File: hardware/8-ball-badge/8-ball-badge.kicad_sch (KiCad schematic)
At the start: 76 parts, among them J1 BattConn, J2 SAO Header 1, J3 SAO Header 2, Q1 AO3401A, Q2 S8050, SW1 SW_Push, SW2 TS-1187A-B-A-B, U1 TC4056A, U10 ME6210A33PG, U2 W25Q128JVSIQTR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

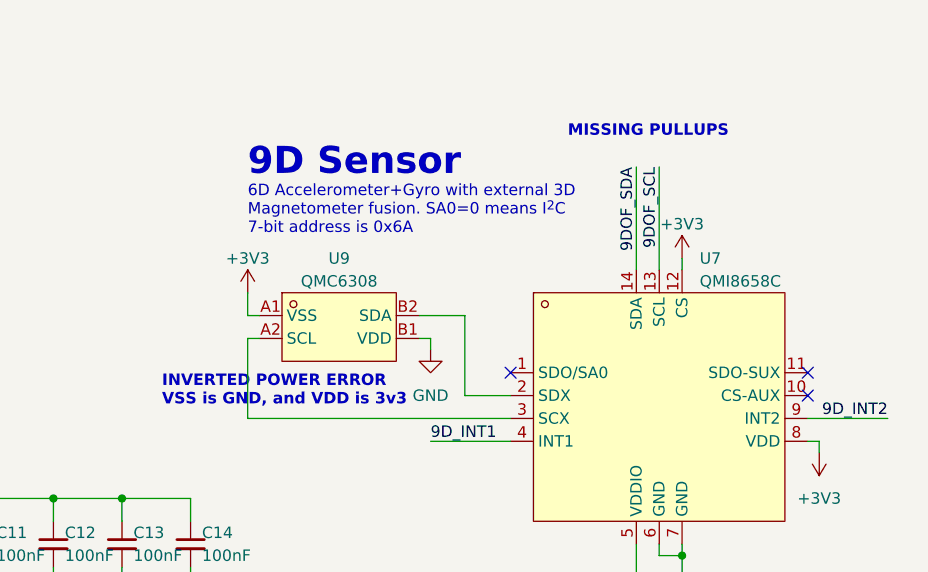
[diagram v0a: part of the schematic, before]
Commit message: Fix issues with 9DoF chip
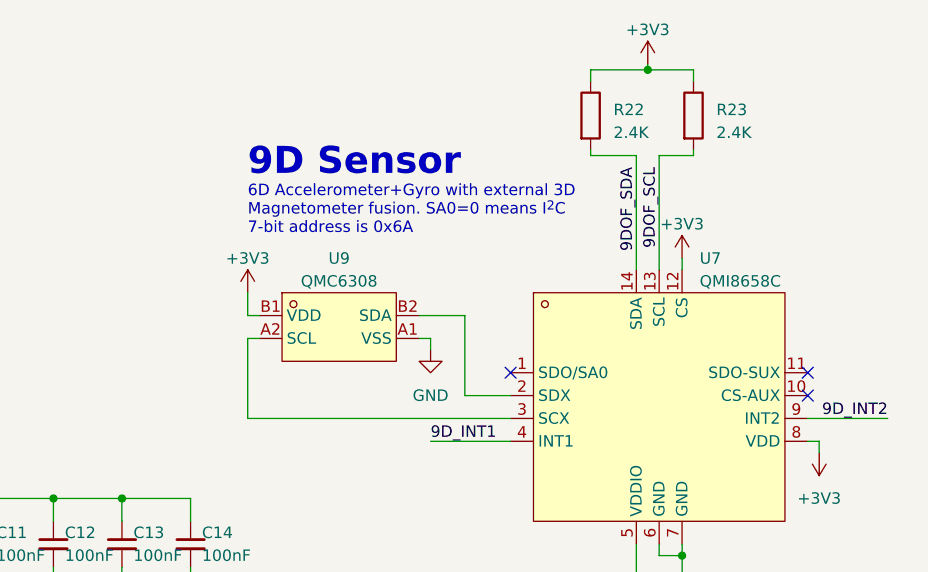
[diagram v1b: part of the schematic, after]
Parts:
- added R22, R23: 2.4K, Resistor_SMD:R_0603_1608Metric_Pad0.98x0.95mm_HandSolder, symbol Device:R
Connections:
- net +3V3: now also U9.B1 (VDD), R22.1, R23.1; no longer U9.A1 (VSS)
- net 9DOF_SCL: now also R23.2
- net 9DOF_SDA: now also R22.2
- net GND: now also U9.A1 (VSS); no longer U9.B1 (VDD)
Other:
- note removed: "INVERTED POWER ERROR VSS is GND, and VDD is 3v3"
- note removed: "MISSING PULLUPS"
- company: (none) -> Designed by Tyler Crumpton (CrumpSpace)
- title: (none) -> Magic 8-Badge
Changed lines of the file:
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@@
 (kicad_sch (version 20230121) (generator eeschema)
   (paper "A3")
+  (title_block
+    (title "Magic 8-Badge")
+    (date "2023-11-04")
+    (rev "v1 ")
+    (company "Designed by Tyler Crumpton (CrumpSpace)")
+    (comment 1 "Copyright Tyler Crumpton, 2023 ")
+    (comment 2 "Licensed under CERN-OHL-P version 2")
+    (comment 3 "PhreakNIC 2023 Edition")
+  )
   (junction (at 289.56 176.53) (diameter 0) (color 0 0 0 0)
   )
@@
   (junction (at 215.9 115.57) (diameter 0) (color 0 0 0 0)
   )
+  (junction (at 234.95 20.955) (diameter 0) (color 0 0 0 0)
+  )
   (junction (at 43.18 160.02) (diameter 0) (color 0 0 0 0)
   )
@@
     (stroke (width 0) (type default))
   )
+  (wire (pts (xy 234.95 20.955) (xy 234.95 20.32))
+    (stroke (width 0) (type default))
+  )
   (wire (pts (xy 271.78 72.39) (xy 271.78 73.66))
     (stroke (width 0) (type default))
@@
     (stroke (width 0) (type default))
   )
+  (wire (pts (xy 240.03 30.48) (xy 240.03 29.845))
+    (stroke (width 0) (type default))
+  )
   (wire (pts (xy 191.77 50.8) (xy 190.5 50.8))
     (stroke (width 0) (type default))
@@
     (stroke (width 0) (type default))
   )
+  (wire (pts (xy 236.22 30.48) (xy 240.03 30.48))
+    (stroke (width 0) (type default))
+  )
   (wire (pts (xy 82.55 119.38) (xy 85.09 119.38))
     (stroke (width 0) (type default))
@@
     (stroke (width 0) (type default))
   )
-  (wire (pts (xy 233.68 31.75) (xy 233.68 43.18))
+  (wire (pts (xy 233.68 30.48) (xy 233.68 43.18))
     (stroke (width 0) (type default))
   )
@@
     (stroke (width 0) (type default))
   )
-  (wire (pts (xy 236.22 31.75) (xy 236.22 43.18))
+  (wire (pts (xy 236.22 30.48) (xy 236.22 43.18))
     (stroke (width 0) (type default))
   )
@@
     (stroke (width 0) (type default))
   )
+  (wire (pts (xy 233.68 30.48) (xy 228.6 30.48))
+    (stroke (width 0) (type default))
+  )
   (wire (pts (xy 96.52 87.63) (xy 96.52 91.44))
     (stroke (width 0) (type default))
@@
     (stroke (width 0) (type default))
   )
+  (wire (pts (xy 234.95 20.955) (xy 240.03 20.955))
+    (stroke (width 0) (type default))
+  )
   (wire (pts (xy 209.55 48.26) (xy 214.63 48.26))
     (stroke (width 0) (type default))
@@
     (stroke (width 0) (type default))
   )
+  (wire (pts (xy 228.6 22.225) (xy 228.6 20.955))
+    (stroke (width 0) (type default))
+  )
   (wire (pts (xy 246.38 181.61) (xy 240.03 181.61))
     (stroke (width 0) (type default))
@@
     (stroke (width 0) (type default))
   )
+  (wire (pts (xy 228.6 20.955) (xy 234.95 20.955))
+    (stroke (width 0) (type default))
+  )
   (wire (pts (xy 198.12 115.57) (xy 199.39 115.57))
     (stroke (width 0) (type default))
@@
     (stroke (width 0) (type default))
   )
+  (wire (pts (xy 240.03 20.955) (xy 240.03 22.225))
+    (stroke (width 0) (type default))
+  )
   (wire (pts (xy 283.21 171.45) (xy 281.94 171.45))
     (stroke (width 0) (type default))
@@
     (stroke (width 0) (type default))
   )
+  (wire (pts (xy 228.6 29.845) (xy 228.6 30.48))
+    (stroke (width 0) (type default))
+  )
   (wire (pts (xy 50.8 152.4) (xy 43.18 152.4))
     (stroke (width 0) (type default))
@@
     (effects (font (face "Rockwell") (size 3 3) (thickness 0.254) bold) (justify left bottom))
   )
-  (text "INVERTED POWER ERROR\nVSS is GND, and VDD is 3v3" (at 180.975 58.42 0)
-    (effects (font (size 1.27 1.27) (thickness 0.254) bold (color 255 5 28 1)) (justify left bottom))
-  )
   (text "9D Sensor" (at 190.5 33.02 0)
     (effects (font (face "Rockwell") (size 3 3) (thickness 0.254) bold) (justify left bottom))
@@
     (effects (font (face "Rockwell") (size 3 3) (thickness 0.254) bold) (justify left bottom))
   )
-  (text "MISSING PULLUPS" (at 226.06 28.575 0)
-    (effects (font (size 1.27 1.27) (thickness 0.254) bold (color 255 5 28 1)) (justify left bottom))
-  )
   (text "Simple LDO regulator, with a drop-out voltage\nof 220mV at 200mA. It will provide 3.3V output\nwith an input as low as 3.5V."
     (at 187.96 106.68 0)
@@
     )
   )
+  (symbol (lib_id "power:+3V3") (at 234.95 20.32 0) (unit 1)
+    (in_bom yes) (on_board yes) (dnp no) (fields_autoplaced)
+    (property "Reference" "#PWR051" (at 234.95 24.13 0)
+      (effects (font (face "Rockwell") (size 1.27 1.27)) hide)
+    )
+    (property "Value" "+3V3" (at 234.95 16.51 0)
+      (effects (font (face "Rockwell") (size 1.27 1.27)))
+    )
+    (property "Footprint" "" (at 234.95 20.32 0)
+      (effects (font (face "Rockwell") (size 1.27 1.27)) hide)
+    )
+    (property "Datasheet" "" (at 234.95 20.32 0)
+      (effects (font (face "Rockwell") (size 1.27 1.27)) hide)
+    )
+    (pin "1")
+    (instances
+      (project "8-ball-badge"
+        (path "/191a0ba0-5f5b-4280-b4d9-fca72ce600bc"
+          (reference "#PWR051") (unit 1)
+        )
+      )
+    )
+  )
   (symbol (lib_id "power:GND") (at 35.56 105.41 0) (unit 1)
     (in_bom yes) (on_board yes) (dnp no) (fields_autoplaced)
@@
     )
   )
+  (symbol (lib_id "Device:R") (at 240.03 26.035 0) (unit 1)
+    (in_bom yes) (on_board yes) (dnp no) (fields_autoplaced)
+    (property "Reference" "R23" (at 242.57 25.3999 0)
+      (effects (font (face "Rockwell") (size 1.27 1.27)) (justify left))
+    )
+    (property "Value" "2.4K" (at 242.57 27.9399 0)
+      (effects (font (face "Rockwell") (size 1.27 1.27)) (justify left))
+    )
+    (property "Footprint" "Resistor_SMD:R_0603_1608Metric_Pad0.98x0.95mm_HandSolder" (at 238.252 26.035 90)
+      (effects (font (face "Rockwell") (size 1.27 1.27)) hide)
+    )
+    (property "Datasheet" "~" (at 240.03 26.035 0)
+      (effects (font (face "Rockwell") (size 1.27 1.27)) hide)
+    )
+    (property "LCSC Part #" "C22940" (at 240.03 26.035 0)
+      (effects (font (size 1.27 1.27)) hide)
+    )
+    (pin "1")
+    (pin "2")
+    (instances
+      (project "8-ball-badge"
+        (path "/191a0ba0-5f5b-4280-b4d9-fca72ce600bc"
+          (reference "R23") (unit 1)
+        )
+      )
+    )
+  )
   (symbol (lib_id "power:GND") (at 217.17 195.58 0) (unit 1)
     (in_bom yes) (on_board yes) (dnp no) (fields_autoplaced)
@@
         )
       )
+    )
+  )
+  (symbol (lib_id "Device:R") (at 228.6 26.035 0) (unit 1)
+    (in_bom yes) (on_board yes) (dnp no) (fields_autoplaced)
+    (property "Reference" "R22" (at 231.14 25.3999 0)
+      (effects (font (face "Rockwell") (size 1.27 1.27)) (justify left))
+    )
+    (property "Value" "2.4K" (at 231.14 27.9399 0)
+      (effects (font (face "Rockwell") (size 1.27 1.27)) (justify left))
+    )
+    (property "Footprint" "Resistor_SMD:R_0603_1608Metric_Pad0.98x0.95mm_HandSolder" (at 226.822 26.035 90)
+      (effects (font (face "Rockwell") (size 1.27 1.27)) hide)
+    )
+    (property "Datasheet" "~" (at 228.6 26.035 0)
+      (effects (font (face "Rockwell") (size 1.27 1.27)) hide)
+    )
+    (property "LCSC Part #" "C22940" (at 228.6 26.035 0)
+      (effects (font (size 1.27 1.27)) hide)
+    )
+    (pin "1")
+    (pin "2")
+    (instances
+      (project "8-ball-badge"
+        (path "/191a0ba0-5f5b-4280-b4d9-fca72ce600bc"
+          (reference "R22") (unit 1)
+        )
+      )
